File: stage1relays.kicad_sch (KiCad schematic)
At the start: 14 parts, among them T3 AO3400A, T4 AO3400A

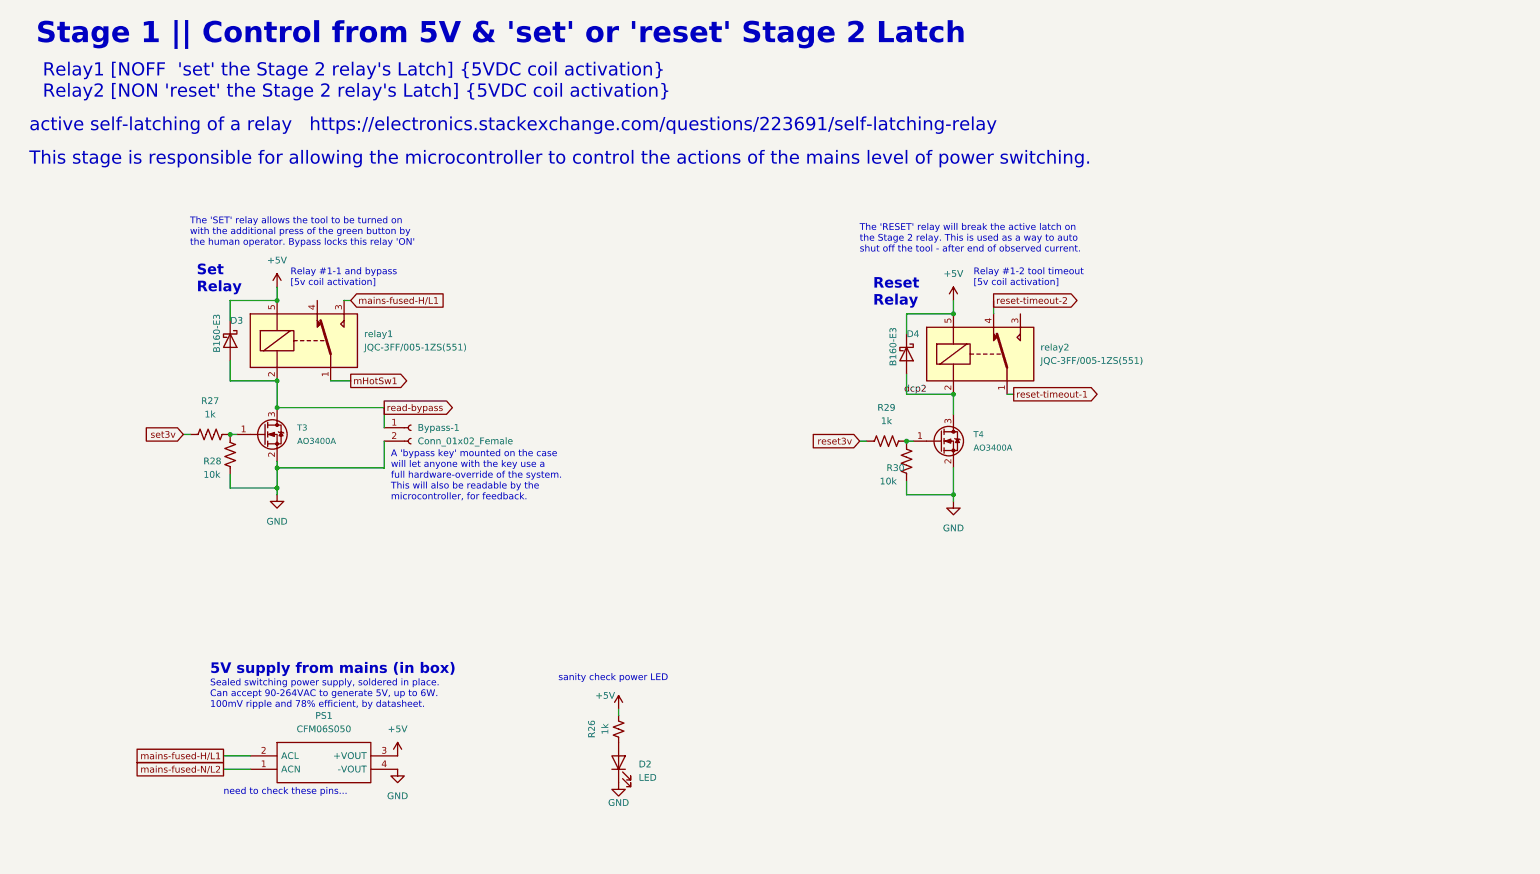
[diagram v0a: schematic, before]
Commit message: double-check mains connections, update notes
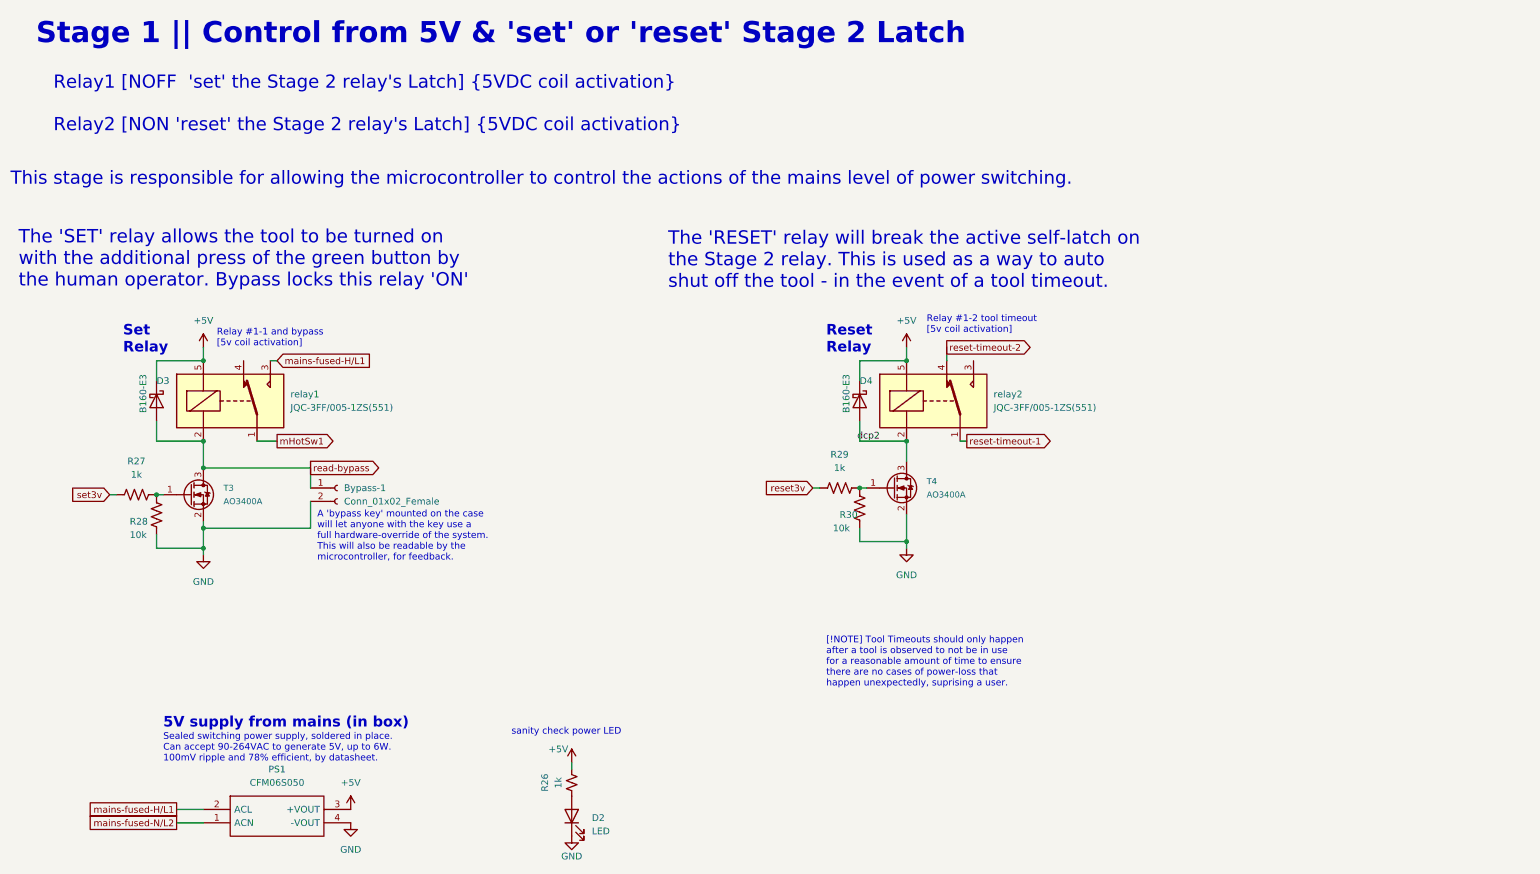
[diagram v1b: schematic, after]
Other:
- note added: "The 'RESET' relay will break the active self-latch on the Stage 2 relay. This is used as a way to auto shut off the tool - in the event of a tool timeout."
- note added: "[!NOTE] Tool Timeouts should only happen after a tool is observed to not be in use for a reasonable amount of time to ensure there are no cases of power-loss that happen unexpectedly, suprising a user."
- note removed: "The 'RESET' relay will break the active latch on the Stage 2 relay. This is used as a way to auto shut off the tool - after end of observed current."
- note removed: "active self-latching of a relay https://electronics.stackexchange.com/questions/223691/self-latching-relay"
- note removed: "need to check these pins..."
- moved on the sheet: Bypass-1, D2, D3, D4, PS1, R26, R27, R28, R29, R30, T3, T4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

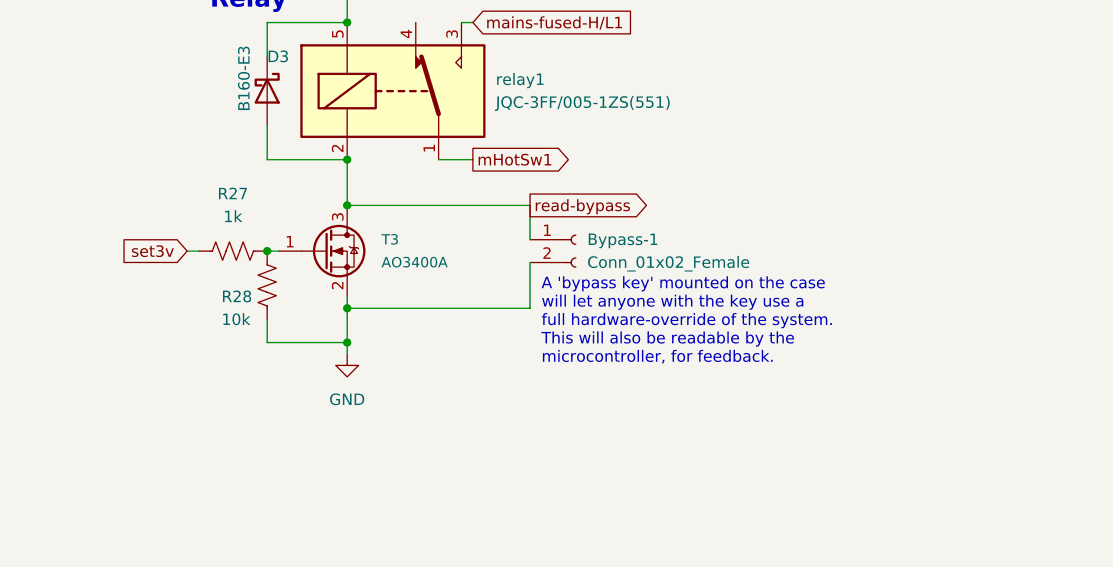
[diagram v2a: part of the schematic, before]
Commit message: candidate reconfiguration for bypass key operation and sensing
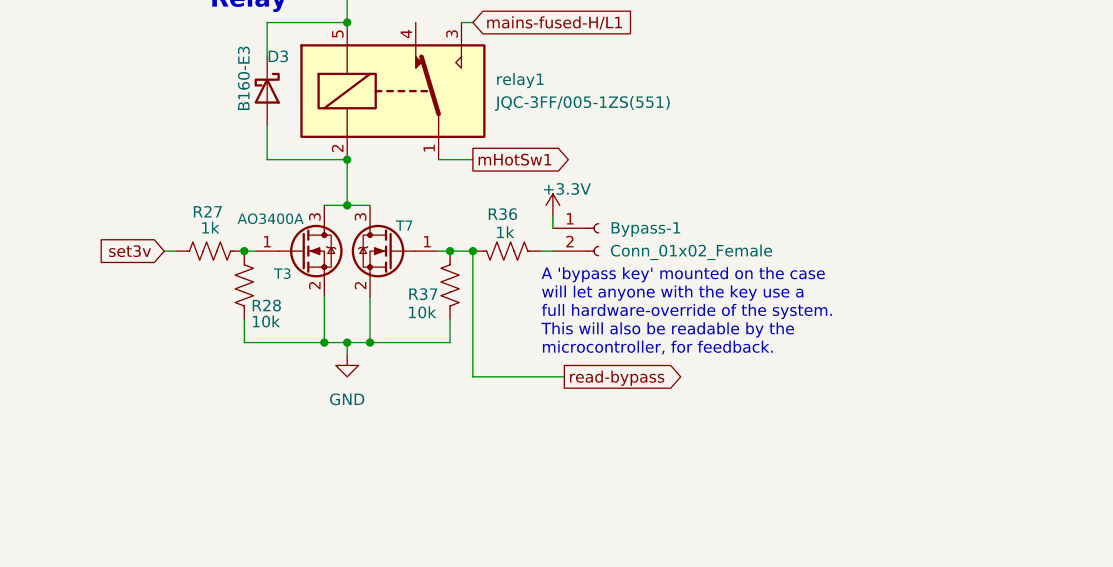
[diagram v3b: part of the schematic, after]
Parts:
- added R36: 1k, Resistor_SMD:R_0603_1608Metric, symbol Device:R_US
- added R37: 10k, Resistor_SMD:R_0603_1608Metric, symbol Device:R_US
- added T7: AO3400A, Package_TO_SOT_SMD:SOT-23, symbol Transistor_FET:AO3400A
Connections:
- net GND: now also R37.2, T7.2 (S); no longer Bypass-1.2 (Pin_2)
- net read-bypass: now also R36.2, R37.1, T7.1 (G); no longer Bypass-1.1 (Pin_1), D3.2 (A), T3.3 (D), relay1.2
- new net: D3.2 (A), T3.3 (D), T7.3 (D), relay1.2
- new net: Bypass-1.2 (Pin_2), R36.1
- new net +3.3V: Bypass-1.1 (Pin_1)
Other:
- moved on the sheet: Bypass-1, R27, R28, T3

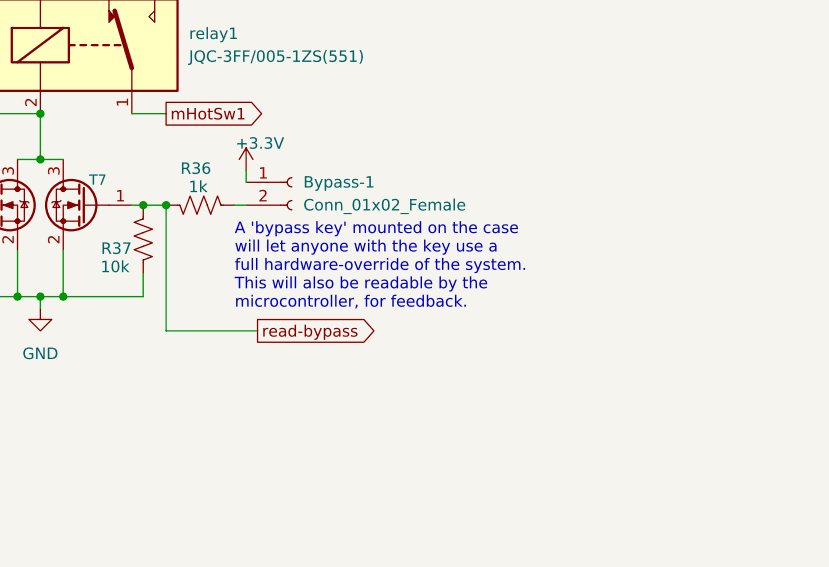
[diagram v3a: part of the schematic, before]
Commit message: reassigned netclasses, removed vestigial level-shifter
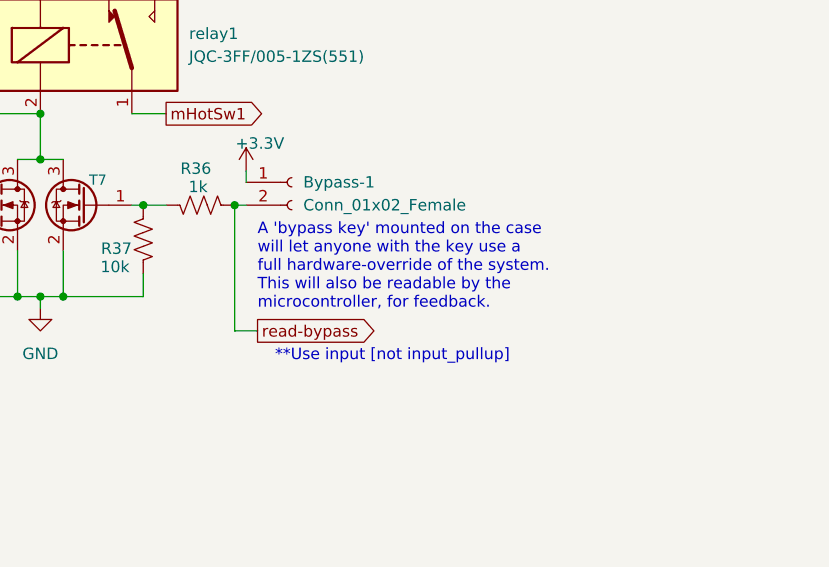
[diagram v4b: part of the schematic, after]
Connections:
- net read-bypass: now also Bypass-1.2 (Pin_2), R36.1; no longer R36.2, R37.1, T7.1 (G)
- new net: R36.2, R37.1, T7.1 (G)
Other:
- note added: "**Use input [not input_pullup]"
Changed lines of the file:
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@@
-	)
-	(junction
-		(at 73.66 114.3)
-		(diameter 0)
-		(color 0 0 0 0)
 	)
 	(junction
@@
 	)
 	(junction
+		(at 81.28 114.3)
+		(diameter 0)
+		(color 0 0 0 0)
+	)
+	(junction
 		(at 193.04 88.9)
 		(diameter 0)
@@
 	(wire
 		(pts
-			(xy 73.66 128.27) (xy 73.66 114.3)
-		)
-		(stroke
-			(width 0)
-			(type default)
-		)
-	)
-	(wire
-		(pts
 			(xy 59.69 109.22) (xy 62.23 109.22)
 		)
@@
 	(wire
 		(pts
+			(xy 81.28 114.3) (xy 81.28 128.27)
+		)
+		(stroke
+			(width 0)
+			(type default)
+		)
+	)
+	(wire
+		(pts
+			(xy 81.28 128.27) (xy 83.82 128.27)
+		)
+		(stroke
+			(width 0)
+			(type default)
+		)
+	)
+	(wire
+		(pts
 			(xy 57.15 109.22) (xy 59.69 109.22)
 		)
@@
 		)
 	)
-	(wire
-		(pts
-			(xy 73.66 128.27) (xy 83.82 128.27)
-		)
-		(stroke
-			(width 0)
-			(type default)
-		)
-	)
 	(text "The 'SET' relay allows the tool to be turned on\nwith the additional press of the green button by\nthe human operator. Bypass locks this relay 'ON'"
 		(exclude_from_sim no)
@@
 			)
 			(justify left bottom)
+		)
+	)
+	(text "**Use input [not input_pullup]"
+		(exclude_from_sim no)
+		(at 98.806 131.064 0)
+		(effects
+			(font
+				(size 1.27 1.27)
+			)
 		)
 	)
@@
 	(text "A 'bypass key' mounted on the case \nwill let anyone with the key use a \nfull hardware-override of the system. \nThis will also be readable by the \nmicrocontroller, for feedback."
 		(exclude_from_sim no)
-		(at 81.28 125.984 0)
+		(at 83.82 125.984 0)
 		(effects
 			(font
@@
 			)
 		)
+	)
+	(netclass_flag ""
+		(length 2.54)
+		(shape round)
+		(at 81.28 128.27 180)
+		(fields_autoplaced yes)
+		(effects
+			(font
+				(size 1.27 1.27)
+			)
+			(justify right bottom)
+		)
+		(property "Netclass" "Default"
+			(at 80.5815 130.81 0)
+			(effects
+				(font
+					(size 1.27 1.27)
+					(italic yes)
+				)
+				(justify right)
+			)
+		)
+	)
+	(netclass_flag ""
+		(length 2.54)
+		(shape round)
+		(at 60.96 109.22 0)
+		(fields_autoplaced yes)
+		(effects
+			(font
+				(size 1.27 1.27)
+			)
+			(justify left bottom)
+		)
+		(property "Netclass" "DC-Power"
+			(at 61.6585 106.68 0)
+			(effects
+				(font
+					(size 1.27 1.27)
+					(italic yes)
+				)
+				(justify left)
+			)
+		)

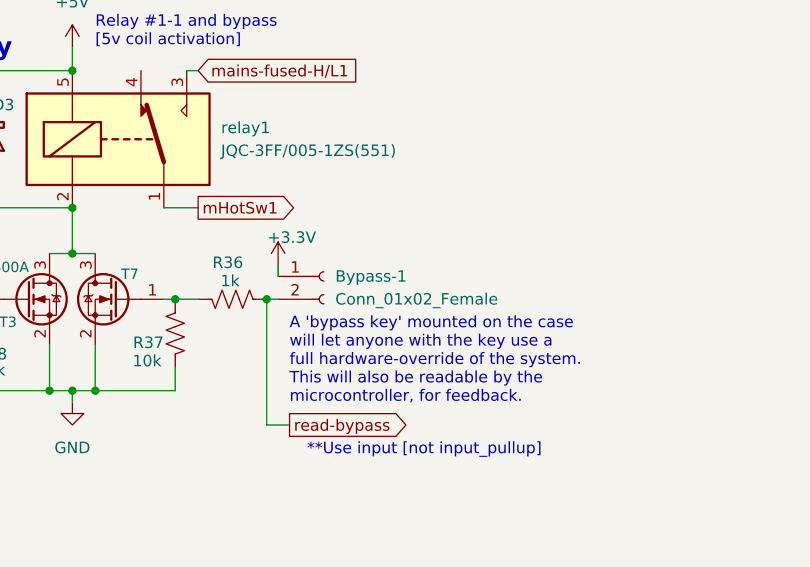
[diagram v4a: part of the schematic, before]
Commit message: flip pins on bypass key for better wire-routing
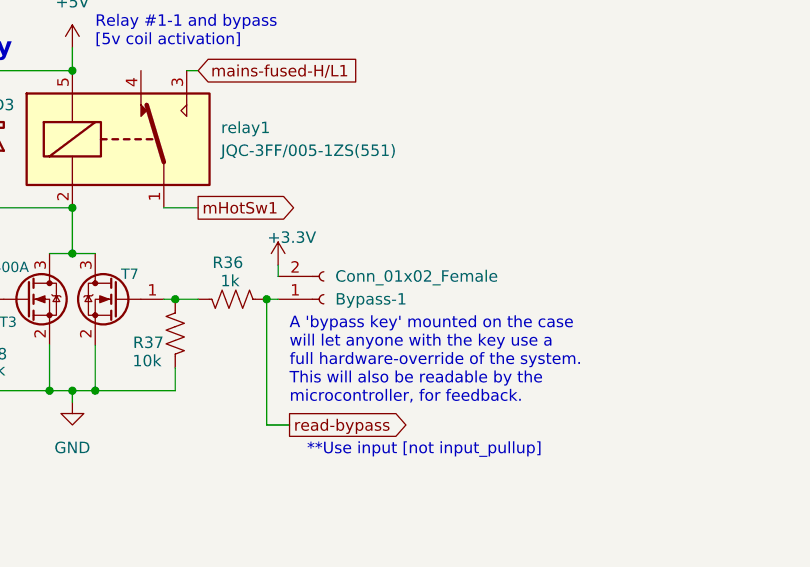
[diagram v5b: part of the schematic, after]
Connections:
- net +3.3V: now also Bypass-1.2 (Pin_2); no longer Bypass-1.1 (Pin_1)
- net read-bypass: now also Bypass-1.1 (Pin_1); no longer Bypass-1.2 (Pin_2)
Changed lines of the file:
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@@
 	(symbol
 		(lib_id "Connector:Conn_01x02_Female")
-		(at 87.63 111.76 0)
+		(at 87.63 114.3 0)
+		(mirror x)
 		(unit 1)
 		(exclude_from_sim no)
@@
 		(dnp no)
 		(property "Reference" "Bypass-1"
-			(at 88.9 111.7599 0)
+			(at 88.9 114.3001 0)
 			(effects
 				(font
@@
 		)
 		(property "Value" "Conn_01x02_Female"
-			(at 88.9 114.2999 0)
+			(at 88.9 111.7601 0)
 			(effects
 				(font
@@
 		)
 		(property "Footprint" "Connector_JST:JST_PH_B2B-PH-K_1x02_P2.00mm_Vertical"
-			(at 87.63 111.76 0)
+			(at 87.63 114.3 0)
 			(effects
 				(font
@@
 		)
 		(property "Datasheet" "~"
-			(at 87.63 111.76 0)
+			(at 87.63 114.3 0)
 			(effects
 				(font
@@
 		)
 		(property "Description" ""
-			(at 87.63 111.76 0)
+			(at 87.63 114.3 0)
 			(effects
 				(font
@@
 		)
 		(property "JLCPCB Part #" "C131337"
-			(at 87.63 111.76 0)
+			(at 87.63 114.3 0)
 			(effects
 				(font
